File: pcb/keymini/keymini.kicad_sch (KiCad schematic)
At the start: 86 parts, among them J1 USB_C_Receptacle_USB2.0_16P, J2 Conn_01x04, SW1A1 SW_Push, SW1B1 SW_Push, SW1C1 SW_Push, SW1D1 SW_Push, SW1E1 SW_Push, SW1F1 SW_Push, SW1G1 SW_Push, SW1H1 SW_Push, SW1I1 SW_Push, SW1J1 SW_Push, SW2A1 SW_Push, SW2B1 SW_Push, SW2C1 SW_Push, SW2D1 SW_Push, SW2E1 SW_Push, SW2F1 SW_Push, SW2G1 SW_Push, SW2H1 SW_Push, SW2I1 SW_Push, SW2J1 SW_Push, SW3A1 SW_Push, SW3B1 SW_Push, SW3C1 SW_Push, SW3D1 SW_Push, SW3E1 SW_Push, SW3F1 SW_Push, SW3G1 SW_Push, SW3H1 SW_Push, SW3I1 SW_Push, SW3J1 SW_Push, SW4C1 SW_Push, SW4D1 SW_Push, SW4E1 SW_Push, SW4F1 SW_Push, SW4G1 SW_Push, SW4H1 SW_Push, U1 STM32F072CBT6, U2 XC6206P332MR

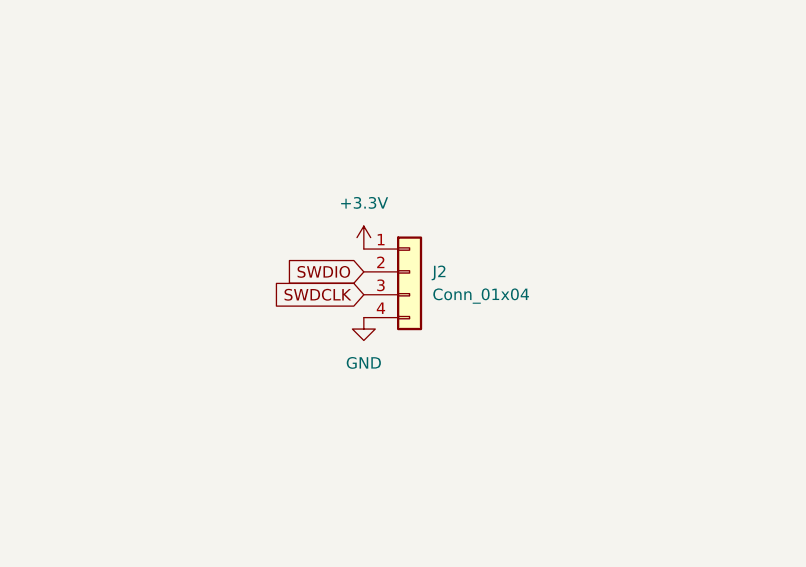
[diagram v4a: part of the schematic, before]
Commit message: Remove SWD connector
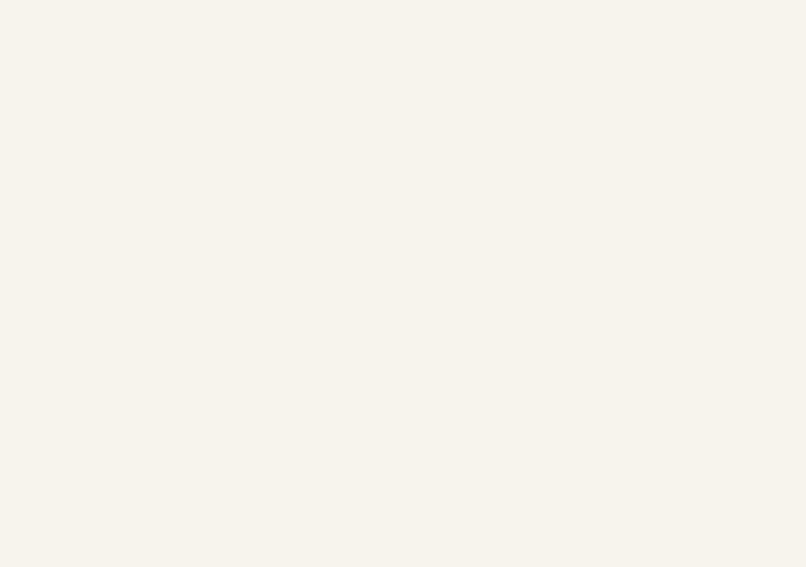
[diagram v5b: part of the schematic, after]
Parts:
- removed J2: Conn_01x04, Connector_Harwin:Harwin_M20-89004xx_1x04_P2.54mm_Horizontal, symbol Connector_Generic:Conn_01x04

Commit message: v0.2 gerber
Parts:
- renumbered BOOT1 to BOOT0
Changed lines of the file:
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@@
 		(dnp no)
 		(fields_autoplaced yes)
-		(property "Reference" "BOOT1"
+		(property "Reference" "BOOT0"
 			(at 213.36 30.48 0)
 			(effects
@@
 			(project ""
 				(path "/5ef0dab6-ab05-4045-8a8e-70c16fe91fb0"
-					(reference "BOOT1")
+					(reference "BOOT0")
 					(unit 1)
 				)
